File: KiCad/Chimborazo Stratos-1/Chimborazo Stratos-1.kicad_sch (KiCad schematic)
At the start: 0 parts

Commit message: fixed long path errors and cleaned up libraries, finally I added the libs for the project it was REALLY HARD AND I DONT KNOW WHY :( but I managed to overcome the challenge
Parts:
- added U1: RP2040, Package_DFN_QFN:QFN-56-1EP_7x7mm_P0.4mm_EP3.2x3.2mm, symbol MCU_RaspberryPi:RP2040
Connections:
- new net: U1.1 (IOVDD), U1.10 (IOVDD), U1.22 (IOVDD), U1.33 (IOVDD), U1.42 (IOVDD), U1.49 (IOVDD)
- new net: U1.23 (DVDD), U1.50 (DVDD)
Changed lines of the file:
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@@
 	(generator_version "9.0")
 	(paper "A4")
+	(symbol
+		(lib_id "MCU_RaspberryPi:RP2040")
+		(at 140.97 80.01 0)
+		(unit 1)
+		(exclude_from_sim no)
+		(in_bom yes)
+		(on_board yes)
+		(dnp no)
+		(fields_autoplaced yes)
+		(property "Reference" "U1"
+			(at 143.1133 124.46 0)
+			(effects
+				(font
+					(size 1.27 1.27)
+				)
+				(justify left)
+			)
+		)
+		(property "Value" "RP2040"
+			(at 143.1133 127 0)
+			(effects
+				(font
+					(size 1.27 1.27)
+				)
+				(justify left)
+			)
+		)
+		(property "Footprint" "Package_DFN_QFN:QFN-56-1EP_7x7mm_P0.4mm_EP3.2x3.2mm"
+			(at 140.97 80.01 0)
+			(effects
+				(font
+					(size 1.27 1.27)
+				)
+				(hide yes)
+			)
+		)
+		(property "Datasheet" "https://datasheets.raspberrypi.com/rp2040/rp2040-datasheet.pdf"
+			(at 140.97 80.01 0)
+			(effects
+				(font
+					(size 1.27 1.27)
+				)
+				(hide yes)
+			)
+		)
+		(property "Description" "A microcontroller by Raspberry Pi"
+			(at 140.97 80.01 0)
+			(effects
+				(font
+					(size 1.27 1.27)
+				)
+				(hide yes)
+			)
+		)
+		(pin "13"
+		)
+		(pin "27"
+		)
+		(pin "20"
+		)
+		(pin "48"
+		)
+		(pin "46"
+		)
+		(pin "55"
+		)
+		(pin "34"
+		)
+		(pin "36"
+		)
+		(pin "38"
+		)
+		(pin "40"
+		)
+		(pin "19"
+		)
+		(pin "56"
+		)
+		(pin "15"
+		)
+		(pin "54"
+		)
+		(pin "10"
+		)
+		(pin "45"
+		)
+		(pin "53"
+		)
+		(pin "42"
+		)
+		(pin "26"
+		)
+		(pin "4"
+		)
+		(pin "47"
+		)
+		(pin "57"
+		)
+		(pin "5"
+		)
+		(pin "51"
+		)
+		(pin "43"
+		)
+		(pin "3"
+		)
+		(pin "33"
+		)
+		(pin "1"
+		)
+		(pin "50"
+		)
+		(pin "2"
+		)
+		(pin "6"
+		)
+		(pin "7"
+		)
+		(pin "9"
+		)
+		(pin "11"
+		)
+		(pin "21"
+		)
+		(pin "8"
+		)
+		(pin "12"
+		)
+		(pin "24"
+		)
+		(pin "25"
+		)
+		(pin "23"
+		)
+		(pin "52"
+		)
+		(pin "49"
+		)
+		(pin "44"
+		)
+		(pin "14"
+		)
+		(pin "22"
+		)
+		(pin "16"
+		)
+		(pin "17"
+		)
+		(pin "18"
+		)
+		(pin "28"
+		)
+		(pin "29"
+		)
+		(pin "30"
+		)
+		(pin "31"
+		)
+		(pin "32"
+		)
+		(pin "35"
+		)
+		(pin "37"
+		)
+		(pin "39"
+		)
+		(pin "41"
+		)
+		(instances
+			(project ""
+				(path "/693bdab5-43ca-4fa8-b8fd-c6e41a7a7cc1"
+					(reference "U1")
+					(unit 1)
+				)
+			)
+		)
+	)
 	(sheet_instances
 		(path "/"

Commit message: Schematic prototype done
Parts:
- removed U1: RP2040, Package_DFN_QFN:QFN-56-1EP_7x7mm_P0.4mm_EP3.2x3.2mm, symbol MCU_RaspberryPi:RP2040
- added J1: BMP280, symbol Connector_Generic:Conn_01x06
- added J2: MPU6050, symbol Connector_Generic:Conn_01x08
- added U1: XIAO-RP2040-DIP, Seeed_Studio_XIAO_Series:XIAO-RP2040-DIP, symbol Seeed_Studio_XIAO_Series:XIAO-RP2040-DIP
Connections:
- new net SCL: J1.4 (Pin_4), J2.4 (Pin_4), U1.6 (P7_SCL_D5)
- new net SDA: J1.5 (Pin_5), J2.5 (Pin_5), U1.5 (P6_SDA_D4)

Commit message: PCB model 1 finalized
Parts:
- added D1: LED, LED_THT:LED_D5.0mm, symbol Device:LED
- added J3, J4: Conn_01x03_Pin, Connector:FanPinHeader_1x03_P2.54mm_Vertical, symbol Connector:Conn_01x03_Pin
- added R1: 220, Resistor_THT:R_Axial_DIN0207_L6.3mm_D2.5mm_P7.62mm_Horizontal, symbol Device:R
- J1: footprint (none) -> Connector_PinHeader_2.54mm:PinHeader_1x06_P2.54mm_Vertical
- J2: footprint (none) -> Connector_PinHeader_2.54mm:PinHeader_1x08_P2.54mm_Vertical
- U1: footprint Seeed_Studio_XIAO_Series:XIAO-RP2040-DIP -> Seeed Studio XIAO Series Library:XIAO-RP2040-DIP
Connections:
- net PWM_1: now reaches U1.1 (P26_A0_D0)
- net PWM_1: now also J4.3 (Pin_3)
- net 3V3: now reaches U1.12 (3V3)
- net 3V3: now also J1.1 (Pin_1), J2.1 (Pin_1)
- net GND: now reaches U1.13 (GND)
- net GND: now also J1.2 (Pin_2), J2.2 (Pin_2), D1.1 (K), J3.1 (Pin_1), J4.1 (Pin_1)
- net VBUS: now reaches U1.14 (VBUS)
- net VBUS: now also J3.2 (Pin_2), J4.2 (Pin_2)
- net PWM_2: now reaches U1.2 (P27_A1_D1)
- net PWM_2: now also J3.3 (Pin_3)
- net at U1.4 (P29_A3_D3): now also R1.1
- new net: D1.2 (A), R1.2
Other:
- moved on the sheet: J1, J2

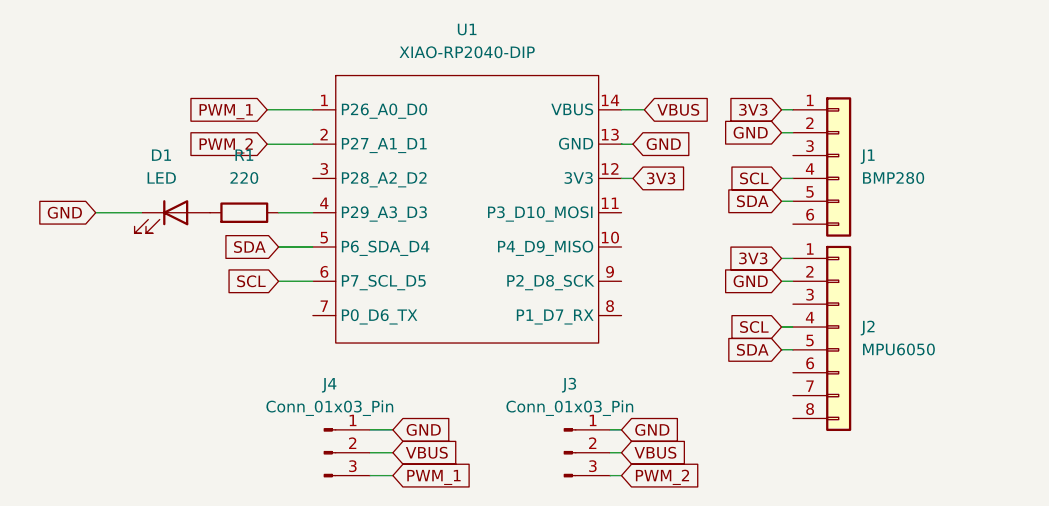
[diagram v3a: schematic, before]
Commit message: Re-work of pcb and CAD model
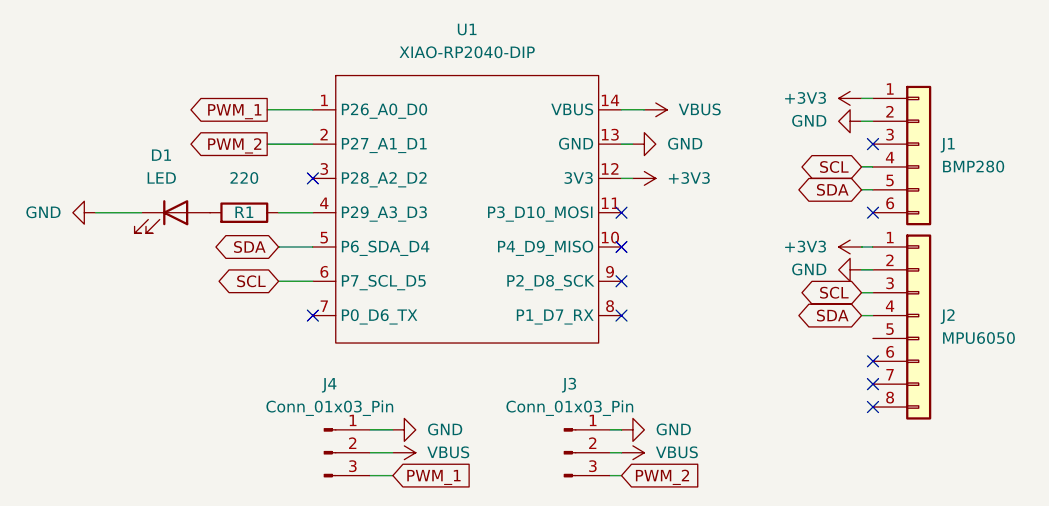
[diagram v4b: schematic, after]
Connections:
- net SCL: now also J2.3 (Pin_3); no longer J2.4 (Pin_4)
- net SDA: now also J2.4 (Pin_4); no longer J2.5 (Pin_5)
- net 3V3 renamed +3V3
- no-connect marks 0 -> 11
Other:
- moved on the sheet: J1, J2

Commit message: Finished the pcb and the cad model REAL NO FAKE
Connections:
- net SCL: now also J1.3 (Pin_3); no longer J1.4 (Pin_4)
- net SDA: now also J1.4 (Pin_4); no longer J1.5 (Pin_5)
- no-connect marks 11 -> 10
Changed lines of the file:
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@@
-	)
-	(no_connect
-		(at 181.61 52.07)
 	)
 	(no_connect
@@
 	(wire
 		(pts
+			(xy 180.34 52.07) (xy 181.61 52.07)
+		)
+		(stroke
+			(width 0)
+			(type default)
+		)
+	)
+	(wire
+		(pts
 			(xy 180.34 54.61) (xy 181.61 54.61)
 		)
@@
 	(wire
 		(pts
-			(xy 180.34 57.15) (xy 181.61 57.15)
-		)
-		(stroke
-			(width 0)
-			(type default)
-		)
-	)
-	(wire
-		(pts
 			(xy 95.25 59.69) (xy 100.33 59.69)
 		)
@@
 			(width 0)
 			(type default)
-		)
-	)
-	(global_label "SDA"
-		(shape bidirectional)
-		(at 180.34 57.15 180)
-		(fields_autoplaced yes)
-		(effects
-			(font
-				(size 1.27 1.27)
-			)
-			(justify right)
-		)
-		(property "Intersheetrefs" "${INTERSHEET_REFS}"
-			(at 172.6754 57.15 0)
-			(effects
-				(font
-					(size 1.27 1.27)
-				)
-				(justify right)
-				(hide yes)
-			)
 		)
 	)
@@
 		)
 	)
+	(global_label "SDA"
+		(shape bidirectional)
+		(at 180.34 54.61 180)
+		(fields_autoplaced yes)
+		(effects
+			(font
+				(size 1.27 1.27)
+			)
+			(justify right)
+		)
+		(property "Intersheetrefs" "${INTERSHEET_REFS}"
+			(at 172.6754 54.61 0)
+			(effects
+				(font
+					(size 1.27 1.27)
+				)
+				(justify right)
+				(hide yes)
+			)
+		)
+	)
+	(global_label "SCL"
+		(shape bidirectional)
+		(at 180.34 52.07 180)
+		(fields_autoplaced yes)
+		(effects
+			(font
+				(size 1.27 1.27)
+			)
+			(justify right)
+		)
+		(property "Intersheetrefs" "${INTERSHEET_REFS}"
+			(at 172.7359 52.07 0)
+			(effects
+				(font
+					(size 1.27 1.27)
+				)
+				(justify right)
+				(hide yes)
+			)
+		)
+	)
 	(global_label "PWM_2"
 		(shape output)
@@
 			(effects
 				(font
-					(size 1.27 1.27)
-				)
-				(justify right)
-				(hide yes)
-			)
-		)
-	)
-	(global_label "SCL"
-		(shape bidirectional)
-		(at 180.34 54.61 180)
-		(fields_autoplaced yes)
-		(effects
-			(font
-				(size 1.27 1.27)
-			)
-			(justify right)
-		)
-		(property "Intersheetrefs" "${INTERSHEET_REFS}"
-			(at 172.7359 54.61 0)
-			(effects
-				(font

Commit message: Reorganized folders and Added the GERBERS files
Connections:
- no-connect marks 10 -> 12
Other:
- moved on the sheet: J1, J2

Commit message: Remade schmeatic changed components and Remade PCB with new and improved layout
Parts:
- removed J1: BMP280, Connector_PinHeader_2.54mm:PinHeader_1x06_P2.54mm_Vertical, symbol Connector_Generic:Conn_01x06
- removed J2: MPU6050, Connector_PinHeader_2.54mm:PinHeader_1x08_P2.54mm_Vertical, symbol Connector_Generic:Conn_01x08
- removed J3, J4: Conn_01x03_Pin, Connector:FanPinHeader_1x03_P2.54mm_Vertical, symbol Connector:Conn_01x03_Pin
- removed U1: XIAO-RP2040-DIP, Seeed Studio XIAO Series Library:XIAO-RP2040-DIP, symbol Seeed_Studio_XIAO_Series:XIAO-RP2040-DIP
- added C2, C5, C6: 100nF, Capacitor_SMD:C_0805_2012Metric, symbol Device:C
- added D2: LED, LED_SMD:LED_0805_2012Metric, symbol Device:LED
- added F1: Polyfuse, Fuse:Fuse_1206_3216Metric, symbol Device:Polyfuse
- added J1: Conn_01x02_Socket, Connector_PinHeader_2.54mm:PinHeader_1x02_P2.54mm_Vertical, symbol Connector:Conn_01x02_Socket
- added JBATTERY1: Conn_01x02, Connector_JST:JST_PH_B2B-PH-K_1x02_P2.00mm_Vertical, symbol Connector_Generic:Conn_01x02
- added JGPS1: Conn_01x04, Connector_PinHeader_2.54mm:PinHeader_1x04_P2.54mm_Vertical, symbol Connector_Generic:Conn_01x04
- added JGY1: Conn_01x10, Connector_PinHeader_2.54mm:PinHeader_1x10_P2.54mm_Vertical, symbol Connector_Generic:Conn_01x10
- added Q1: AO3400A, Package_TO_SOT_SMD:SOT-23, symbol Transistor_FET:AO3400A
- added R2: R, Resistor_SMD:R_0805_2012Metric, symbol Device:R
- added R3, R4: 4.7k, Resistor_SMD:R_0805_2012Metric, symbol Device:R
- added R5: 10k, Resistor_SMD:R_0805_2012Metric, symbol Device:R
- added R6, R7: 1k, Resistor_SMD:R_0805_2012Metric, symbol Device:R
- added Servo1, Servo2: Conn_01x03, Connector_PinHeader_2.54mm:PinHeader_1x03_P2.54mm_Vertical, symbol Connector_Generic:Conn_01x03
- added U1: XIAO-ESP32-C6-SMD, xiaoesp32c6:XIAO-ESP32-C6-SMD, symbol Seeed_Studio_XIAO_Series:XIAO-ESP32-C6-SMD
- D1: footprint LED_THT:LED_D5.0mm -> LED_SMD:LED_0805_2012Metric
- R1: value 220 -> 200k; footprint Resistor_THT:R_Axial_DIN0207_L6.3mm_D2.5mm_P7.62mm_Horizontal -> Resistor_SMD:R_0805_2012Metric
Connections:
- net +3V3: now also C2.1, JGPS1.1 (Pin_1), JGY1.1 (Pin_1), R3.1, R4.1, U1.12 (3V3)
- net GND: now also C2.2, C5.2, C6.2, D2.1 (K), JBATTERY1.2 (Pin_2), JGPS1.4 (Pin_4), JGY1.2 (Pin_2), Q1.2 (S), R2.2, R5.2, Servo1.1 (Pin_1), Servo2.1 (Pin_1), U1.13 (GND), U1.33 (GND)
- net SCL: now also JGY1.3 (Pin_3), R4.2, U1.6 (GPIO23_D5_SCL)
- net SDA: now also JGY1.4 (Pin_4), R3.2, U1.5 (GPIO22_D4_SDA)
- net at D1.2 (A): now also R6.2; no longer R1.2
- net VBAT: now reaches R1.1
- net VBAT: now also C6.1, F1.1, U1.32 (BAT)
- new net: D2.2 (A), R7.2
- new net: J1.2 (Pin_2), Q1.3 (D)
- new net: F1.2, JBATTERY1.1 (Pin_1)
- new net +5V: C5.1, J1.1 (Pin_1), Servo1.3 (Pin_3), Servo2.3 (Pin_3), U1.14 (VBUS)
- new net BAT_SENSE: R1.2, R2.1, U1.1 (GPIO0_A0_D0)
- new net GPS_RX: JGPS1.2 (Pin_2), U1.8 (GPIO17_D7_RX)
- new net GPS_TX: JGPS1.3 (Pin_3), U1.7 (GPIO16_D6_TX)
- new net LED_ARMED: R6.1, U1.10 (GPIO20_D9_MISO)
- new net LED_ERROR: R7.1, U1.11 (GPIO18_D10_MOSI)
- new net PYRO_GATE: Q1.1 (G), R5.1, U1.4 (GPIO21_D3)
- new net SERVO1: Servo1.2 (Pin_2), U1.2 (GPIO1_A1_D1)
- new net SERVO2: Servo2.2 (Pin_2), U1.3 (GPIO2_A2_D2)
- no-connect marks 12 -> 15

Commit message: Added BOM firmware, CAD, Schematic update, and more Images
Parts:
- renumbered J1 to JPyro1
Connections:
- net BAT_SENSE: now also C6.1
- net GND: now also U1.24 (GND); no longer U1.33 (GND)
- net VBAT: now also U1.23 (BAT); no longer C6.1, U1.32 (BAT)
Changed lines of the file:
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@@
-	)
-	(label "VBAT"
-		(at 132.08 82.55 180)
-		(effects
-			(font
-				(size 0.635 0.635)
-			)
-			(justify right bottom)
-		)
 	)
 	(label "VBAT"
@@
 		)
 	)
+	(label "BAT_SENSE"
+		(at 132.08 82.55 180)
+		(effects
+			(font
+				(size 0.635 0.635)
+			)
+			(justify right bottom)
+		)
+	)
 	(label "PYRO_GATE"
 		(at 101.6 34.29 180)
@@
 		(pin "11"
 		)
-		(pin "27"
+		(pin "13"
 		)
 		(pin "9"
@@
 		(pin "3"
 		)
-		(pin "31"
+		(pin "21"
 		)
 		(pin "24"
 		)
-		(pin "32"
-		)
-		(pin "30"
+		(pin "17"
+		)
+		(pin "20"
 		)
 		(pin "14"
@@
 		(pin "10"
 		)
-		(pin "33"
-		)
-		(pin "29"
+		(pin "23"
+		)
+		(pin "19"
 		)
 		(pin "13"
@@
 		(pin "8"
 		)
-		(pin "25"
-		)
-		(pin "28"
+		(pin "16"
+		)
+		(pin "18"
 		)
 		(pin "4"
@@
 		(pin "1"
 		)
-		(pin "26"
+		(pin "15"
 		)
 		(instances
@@
 		(dnp no)
 		(fields_autoplaced yes)
-		(property "Reference" "J1"
+		(property "Reference" "JPyro1"
 			(at 130.81 22.8599 0)
 			(show_name no)
@@
 			(project "Chimborazo Stratos-1"
 				(path "/693bdab5-43ca-4fa8-b8fd-c6e41a7a7cc1"
-					(reference "J1")
-					(unit 1)
-				)
+					(reference "JPyro1")
+					(unit 1)
+				)
